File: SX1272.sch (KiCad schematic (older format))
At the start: 33 parts, among them J8 SMA, U7 SX1272, U8 PE4259, Y2 Crystal

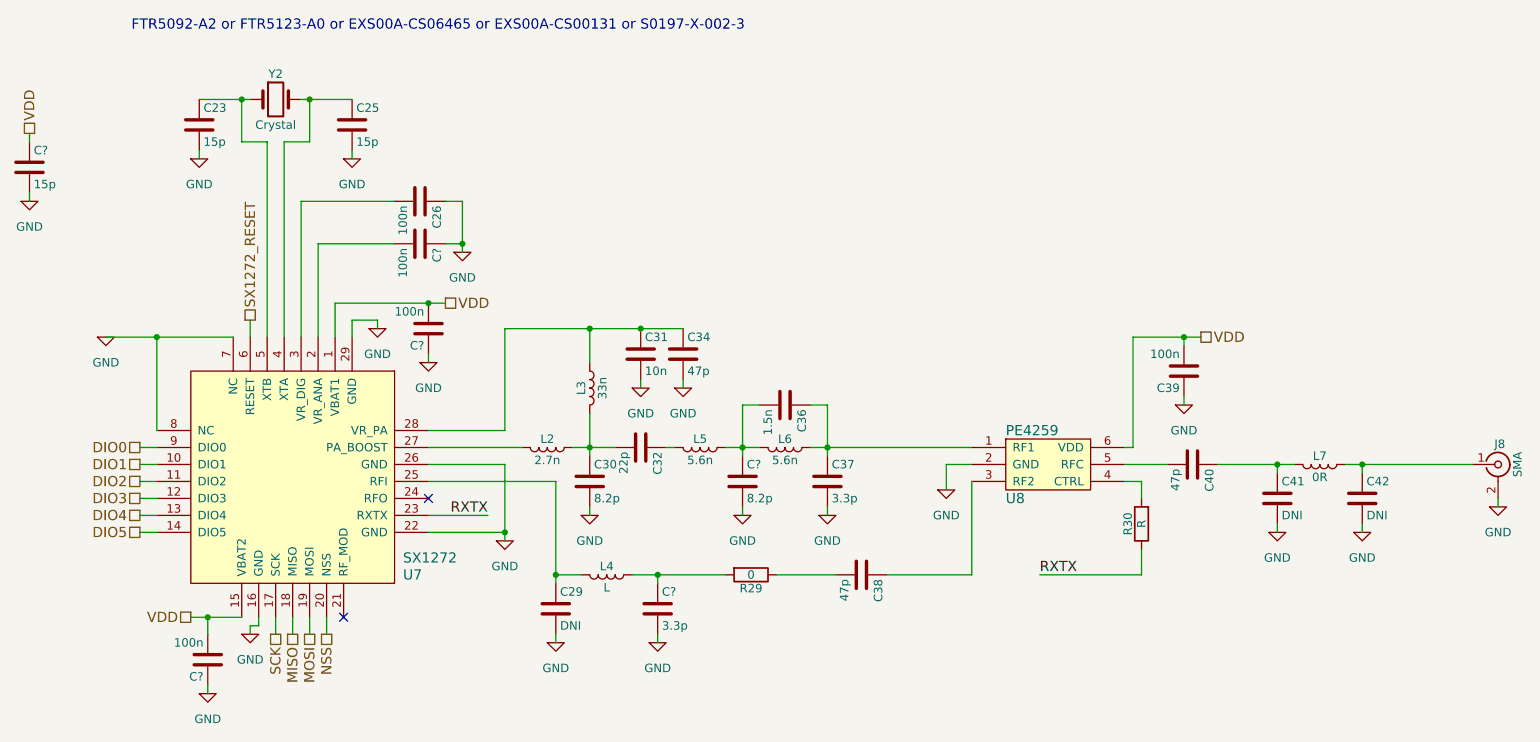
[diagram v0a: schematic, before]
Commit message: Most components arranged on PCB
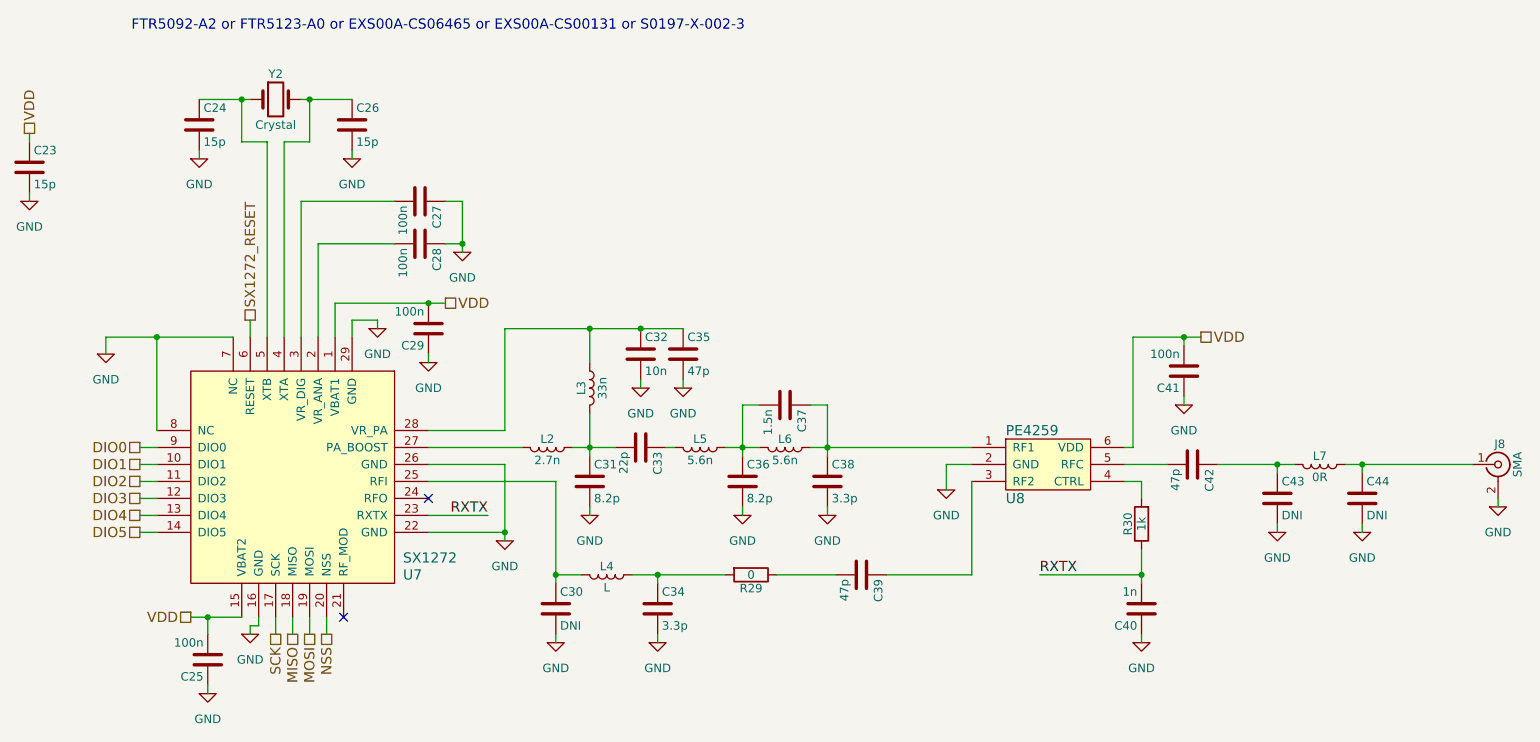
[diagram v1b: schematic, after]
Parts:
- removed C25: 15p, symbol C
- added C26: 15p, Capacitors_SMD:C_0805_HandSoldering, symbol C
- added C40: 1n, Capacitors_SMD:C_0805_HandSoldering, symbol C
- C24: renamed from C23; footprint (none) -> Capacitors_SMD:C_0805_HandSoldering
- C25: renamed from C?; footprint Capacitors_SMD:C_0402_NoSilk -> Capacitors_SMD:C_0805_NoSilk
- J8: footprint footprints:RP-SMA -> tracking_device:RP-SMA
- L2, L3, L4, L5, L6, L7: footprint footprints:L_0402_NoSilk -> tracking_device:L_0402_NoSilk
- R30: value R -> 1k
- U8: footprint footprints:SOT-363_SC-70-6_Handsoldering -> tracking_device:SOT-363_SC-70-6_Handsoldering
- Y2: footprint (none) -> Crystals:Crystal_SMD_2012-2pin_2.0x1.2mm_HandSoldering
- gave numbers to parts that had none: 5
- renumbered C26 to C27, C29 to C30, C30 to C31, C31 to C32, C32 to C33, C34 to C35, C36 to C37, C37 to C38, C38 to C39, C39 to C41, C40 to C42, C41 to C43, C42 to C44
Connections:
- net GND: now also C26.2, C40.1
- net RXTX: now also C40.2
- net at U7.4 (XTA), Y2.2: now also C26.1

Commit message: Added RFM95W
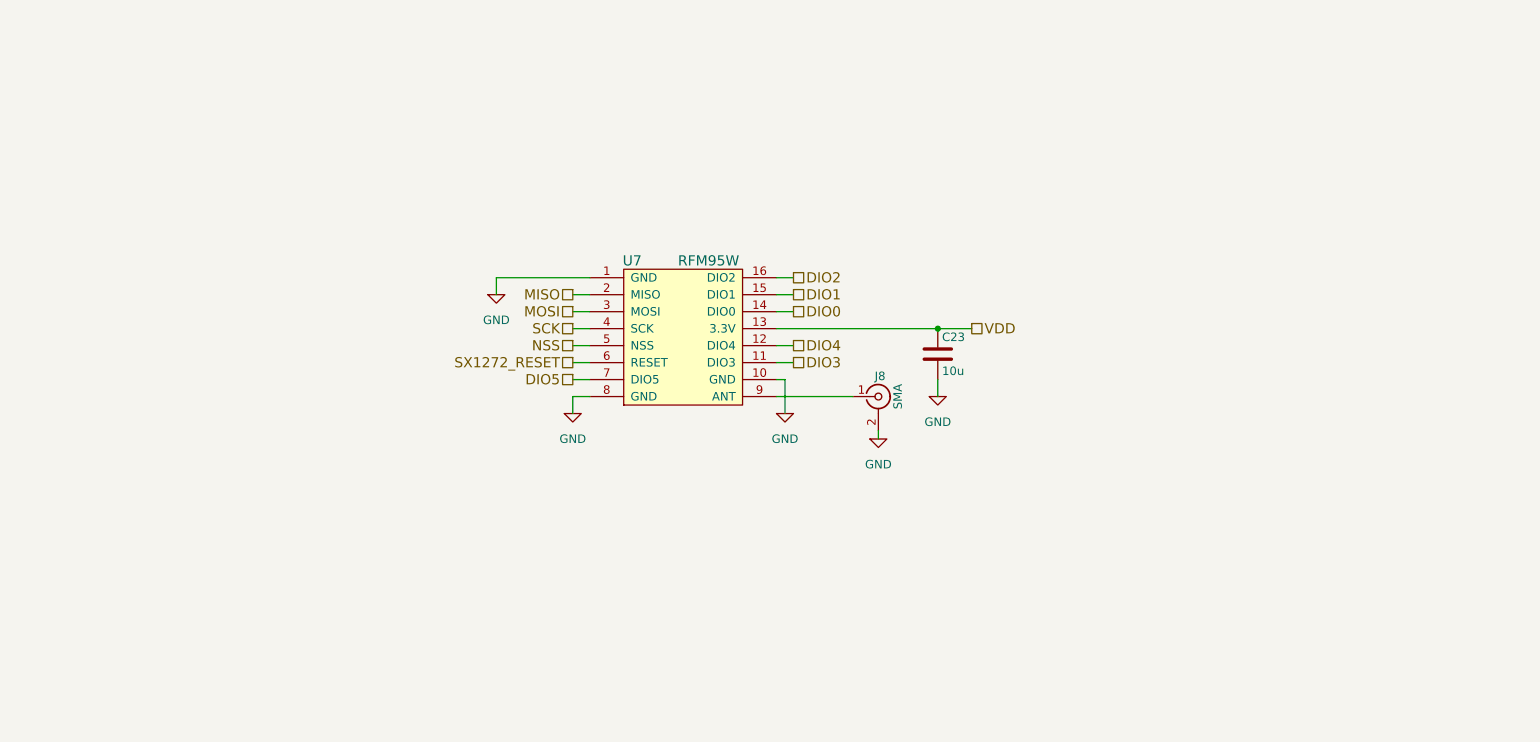
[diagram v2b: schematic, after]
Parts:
- removed C24, C26: 15p, Capacitors_SMD:C_0805_HandSoldering, symbol C
- removed C25: 100n, Capacitors_SMD:C_0805_NoSilk, symbol C
- removed C27, C28, C29, C41: 100n, Capacitors_SMD:C_0402_NoSilk, symbol C
- removed C30, C43, C44: DNI, Capacitors_SMD:C_0402_NoSilk, symbol C
- removed C31, C36: 8.2p, Capacitors_SMD:C_0402_NoSilk, symbol C
- removed C32: 10n, Capacitors_SMD:C_0402_NoSilk, symbol C
- removed C33: 22p, Capacitors_SMD:C_0402_NoSilk, symbol C
- removed C34, C38: 3.3p, Capacitors_SMD:C_0402_NoSilk, symbol C
- removed C35, C42: 47p, Capacitors_SMD:C_0402_NoSilk, symbol C
- removed C37: 1.5n, Capacitors_SMD:C_0402_NoSilk, symbol C
- removed C39: 47p, Resistors_SMD:R_0402_NoSilk, symbol C
- removed C40: 1n, Capacitors_SMD:C_0805_HandSoldering, symbol C
- removed L2: 2.7n, tracking_device:L_0402_NoSilk, symbol L
- removed L3: 33n, tracking_device:L_0402_NoSilk, symbol L
- removed L4: L, tracking_device:L_0402_NoSilk, symbol L
- removed L5, L6: 5.6n, tracking_device:L_0402_NoSilk, symbol L
- removed L7: 0R, tracking_device:L_0402_NoSilk, symbol L
- removed R29: 0, Resistors_SMD:R_0402_NoSilk, symbol R
- removed R30: 1k, Resistors_SMD:R_0805_HandSoldering, symbol R
- removed U7: SX1272, Housings_DFN_QFN:QFN-28-1EP_6x6mm_Pitch0.65mm, symbol SX1272
- removed U8: PE4259, tracking_device:SOT-363_SC-70-6_Handsoldering, symbol PE4259
- removed Y2: Crystal, Crystals:Crystal_SMD_2012-2pin_2.0x1.2mm_HandSoldering, symbol Crystal
- added U7: RFM95W, tracking_device:RFM95W, symbol RFM95W
- C23: value 15p -> 10u
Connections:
- net DIO0: now also U7.14 (DIO0)
- net DIO1: now also U7.15 (DIO1)
- net DIO2: now also U7.16 (DIO2)
- net DIO3: now also U7.11 (DIO3)
- net DIO4: now also U7.12 (DIO4)
- net DIO5: now also U7.7 (DIO5)
- net GND: now also U7.1 (GND), U7.10 (GND), U7.8 (GND)
- net MISO: now also U7.2 (MISO)
- net MOSI: now also U7.3 (MOSI)
- net NSS: now also U7.5 (NSS)
- net SCK: now also U7.4 (SCK)
- net SX1272_RESET: now also U7.6 (RESET)
- net VDD: now also U7.13 (3.3V)
- net at J8.1 (In): now also U7.9 (ANT)
- no-connect marks 2 -> 0
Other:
- note removed: "FTR5092-A2 or FTR5123-A0 or EXS00A-CS06465 or EXS00A-CS00131 or S0197-X-002-3"
- moved on the sheet: J8

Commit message: Version sent out for fabrication
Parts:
- renumbered J8 to J11
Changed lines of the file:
@@
 LIBS:tracking_device
 LIBS:RF_Modules
+LIBS:Electromechanical
+LIBS:Test_Point
+LIBS:electomech-misc
+LIBS:_electromech
+LIBS:Mounting_Hole
 LIBS:tracking_device-cache
 EELAYER 25 0
@@
 SX1272_RESET
 $Comp
-L CONN_COAXIAL J8
+L CONN_COAXIAL J11
 U 1 1 59B49CF4
 P 6200 3550
-F 0 "J8" H 6210 3670 50  0000 C CNN
+F 0 "J11" H 6210 3670 50  0000 C CNN
 F 1 "SMA" V 6315 3550 50  0000 C CNN
 F 2 "tracking_device:RP-SMA" H 6200 3550 50  0001 C CNN
 F 3 "" H 6200 3550 50  0001 C CNN
 	1    6200 3550
-	1    0    0    -1
-$EndComp
-$Comp
-L GND #PWR039
-U 1 1 59B49DE3
-P 6200 3800
-F 0 "#PWR039" H 6200 3550 50  0001 C CNN
-F 1 "GND" H 6200 3650 50  0000 C CNN
-F 2 "" H 6200 3800 50  0001 C CNN
-F 3 "" H 6200 3800 50  0001 C CNN
-	1    6200 3800
 	1    0    0    -1
 $EndComp
@@
 $EndComp
 $Comp
-L GND #PWR040
-U 1 1 59ED90BA
-P 5650 3650
-F 0 "#PWR040" H 5650 3400 50  0001 C CNN
-F 1 "GND" H 5650 3500 50  0000 C CNN
-F 2 "" H 5650 3650 50  0001 C CNN
-F 3 "" H 5650 3650 50  0001 C CNN
-	1    5650 3650
-	1    0    0    -1
-$EndComp
-$Comp
-L GND #PWR041
-U 1 1 59ED90CB
-P 4400 3650
-F 0 "#PWR041" H 4400 3400 50  0001 C CNN
-F 1 "GND" H 4400 3500 50  0000 C CNN
-F 2 "" H 4400 3650 50  0001 C CNN
-F 3 "" H 4400 3650 50  0001 C CNN
-	1    4400 3650
-	1    0    0    -1
-$EndComp
-$Comp
-L GND #PWR042
-U 1 1 59ED90DC
-P 3950 2950
-F 0 "#PWR042" H 3950 2700 50  0001 C CNN
-F 1 "GND" H 3950 2800 50  0000 C CNN
-F 2 "" H 3950 2950 50  0001 C CNN
-F 3 "" H 3950 2950 50  0001 C CNN
-	1    3950 2950
-	1    0    0    -1
-$EndComp
-$Comp
 L C C23
 U 1 1 59EDA1E2
@@
 $EndComp
 Wire Wire Line
-	6200 3800 6200 3750
-Wire Wire Line
 	6050 3550 5600 3550
 Wire Wire Line
-	3950 2950 3950 2850
-Wire Wire Line
-	3950 2850 4500 2850
-Wire Wire Line
-	4400 3650 4400 3550
-Wire Wire Line
-	4400 3550 4500 3550
-Wire Wire Line
-	5650 3650 5650 3450
-Wire Wire Line
-	5650 3450 5600 3450
+	5600 3450 6150 3450
 Wire Wire Line
 	5600 2850 5700 2850
@@
 	4500 2950 4400 2950
 Connection ~ 6550 3150
-$Comp
-L GND #PWR043
-U 1 1 59EDA2EC
-P 6550 3550
-F 0 "#PWR043" H 6550 3300 50  0001 C CNN
-F 1 "GND" H 6550 3400 50  0000 C CNN
-F 2 "" H 6550 3550 50  0001 C CNN
-F 3 "" H 6550 3550 50  0001 C CNN
-	1    6550 3550
-	1    0    0    -1
-$EndComp
 Wire Wire Line
-	6550 3550 6550 3450
+	6550 3850 6550 3450
+Text HLabel 5550 3850 0    60   UnSpc ~ 0
+GND
+Text Label 6100 3850 2    60   ~ 0
+RADIO_GND
+Wire Wire Line
+	5550 3850 6550 3850
+Text Label 6150 3450 2    60   ~ 0
+RADIO_GND
+Text Label 3950 3600 0    60   ~ 0
+RADIO_GND
+Text Label 4000 2850 0    60   ~ 0
+RADIO_GND
+Wire Wire Line
+	4500 2850 4000 2850
+Wire Wire Line
+	4500 3550 4500 3600
+Wire Wire Line
+	4500 3600 3950 3600
+Wire Wire Line
+	6200 3750 6200 3850
+Connection ~ 6200 3850
 $EndSCHEMATC

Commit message: Working on rev 3, started board layout
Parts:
- removed J11: SMA, tracking_device:RP-SMA, symbol CONN_COAXIAL
- added C22, C23: 10u, Capacitors_SMD:C_0805_HandSoldering, symbol C
- added L1: L, Inductors_SMD:L_0805_HandSoldering, symbol L
- renumbered C23 to C24
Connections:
- net at U7.9 (ANT): now also C22.1, L1.2
- net GND renamed RADIO_GND
- net RADIO_GND: now also C22.2, C23.2
- new net ANTENNA: C23.1, L1.1
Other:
- note added: "Antenna from app note DN024 from TI"
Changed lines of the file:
@@
 Text HLabel 4400 3350 0    60   UnSpc ~ 0
 SX1272_RESET
-$Comp
-L CONN_COAXIAL J11
-U 1 1 59B49CF4
-P 6200 3550
-F 0 "J11" H 6210 3670 50  0000 C CNN
-F 1 "SMA" V 6315 3550 50  0000 C CNN
-F 2 "tracking_device:RP-SMA" H 6200 3550 50  0001 C CNN
-F 3 "" H 6200 3550 50  0001 C CNN
-	1    6200 3550
-	1    0    0    -1
-$EndComp
 Text HLabel 4400 3150 0    60   UnSpc ~ 0
 SCK
@@
 VDD
 $Comp
-L RFM95W U7
-U 1 1 59ED83FF
-P 4700 3600
-F 0 "U7" H 4750 4450 60  0000 C CNN
-F 1 "RFM95W" H 5200 4450 60  0000 C CNN
-F 2 "tracking_device:RFM95W" H 5200 4450 60  0001 C CNN
-F 3 "" H 5200 4450 60  0001 C CNN
-	1    4700 3600
-	1    0    0    -1
-$EndComp
-$Comp
-L C C23
+L C C24
 U 1 1 59EDA1E2
 P 6550 3300
-F 0 "C23" H 6575 3400 50  0000 L CNN
+F 0 "C24" H 6575 3400 50  0000 L CNN
 F 1 "10u" H 6575 3200 50  0000 L CNN
 F 2 "Capacitors_SMD:C_0805_HandSoldering" H 6588 3150 50  0001 C CNN
@@
 	1    0    0    -1
 $EndComp
-Wire Wire Line
-	6050 3550 5600 3550
 Wire Wire Line
 	5600 3450 6150 3450
@@
 	4500 2950 4400 2950
 Connection ~ 6550 3150
-Wire Wire Line
-	6550 3850 6550 3450
-Text HLabel 5550 3850 0    60   UnSpc ~ 0
-GND
-Text Label 6100 3850 2    60   ~ 0
-RADIO_GND
-Wire Wire Line
-	5550 3850 6550 3850
 Text Label 6150 3450 2    60   ~ 0
 RADIO_GND
@@
 Wire Wire Line
 	4500 3600 3950 3600
+$Comp
+L RFM95W U7
+U 1 1 59ED83FF
+P 4700 3600
+F 0 "U7" H 4750 4450 60  0000 C CNN
+F 1 "RFM95W" H 5200 4450 60  0000 C CNN
+F 2 "tracking_device:RFM95W" H 5200 4450 60  0001 C CNN
+F 3 "" H 5200 4450 60  0001 C CNN
+	1    4700 3600
+	1    0    0    -1
+$EndComp
+Text Label 7150 3550 2    60   ~ 0
+RADIO_GND
 Wire Wire Line
-	6200 3750 6200 3850
-Connection ~ 6200 3850
+	7150 3550 6550 3550
+Wire Wire Line
+	6550 3550 6550 3450
+Text Label 6900 3850 2    60   ~ 0
+ANTENNA
+Text Notes 3350 5150 0    60   ~ 0
+Antenna from app note DN024 from TI
+$Comp
+L C C23
+U 1 1 5ACC1A63
+P 6400 4050
+F 0 "C23" H 6425 4150 50  0000 L CNN
+F 1 "10u" H 6425 3950 50  0000 L CNN
+F 2 "Capacitors_SMD:C_0805_HandSoldering" H 6438 3900 50  0001 C CNN
+F 3 "" H 6400 4050 50  0001 C CNN
+	1    6400 4050
+	1    0    0    -1
+$EndComp
+$Comp
+L C C22
+U 1 1 5ACC1A98
+P 5900 4050
+F 0 "C22" H 5925 4150 50  0000 L CNN
+F 1 "10u" H 5925 3950 50  0000 L CNN
+F 2 "Capacitors_SMD:C_0805_HandSoldering" H 5938 3900 50  0001 C CNN
+F 3 "" H 5900 4050 50  0001 C CNN
+	1    5900 4050
+	1    0    0    -1
+$EndComp
+$Comp
+L L L1
+U 1 1 5ACC1AC3
+P 6150 3850
+F 0 "L1" V 6100 3850 50  0000 C CNN
+F 1 "L" V 6225 3850 50  0000 C CNN
+F 2 "Inductors_SMD:L_0805_HandSoldering" H 6150 3850 50  0001 C CNN
+F 3 "" H 6150 3850 50  0001 C CNN
+	1    6150 3850
+	0    1    1    0
+$EndComp
+Wire Wire Line
+	6900 3850 6300 3850
+Wire Wire Line
+	6400 3900 6400 3850
+Connection ~ 6400 3850
+Wire Wire Line
+	5900 3900 5900 3850
+Wire Wire Line
+	5600 3850 6000 3850
+Wire Wire Line
+	5600 3850 5600 3550
+Connection ~ 5900 3850
+Text Label 7000 4300 2    60   ~ 0
+RADIO_GND
+Wire Wire Line
+	5900 4300 7000 4300
+Wire Wire Line
+	6400 4300 6400 4200
+Wire Wire Line
+	5900 4300 5900 4200
+Connection ~ 6400 4300
 $EndSCHEMATC

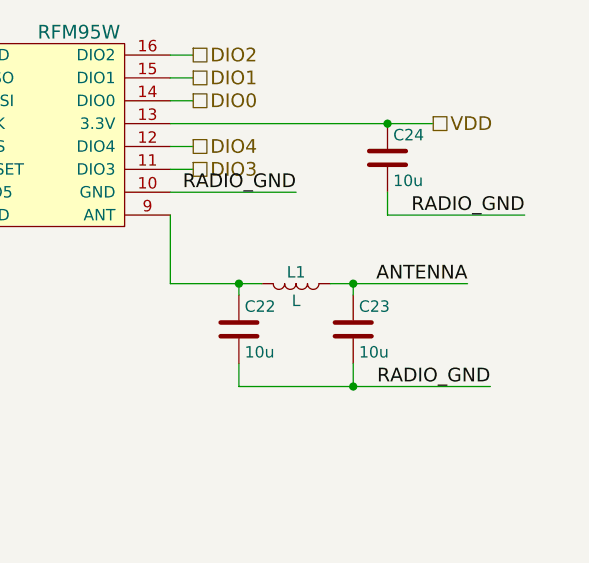
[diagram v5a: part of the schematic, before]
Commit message: Rev 3 DRC clean
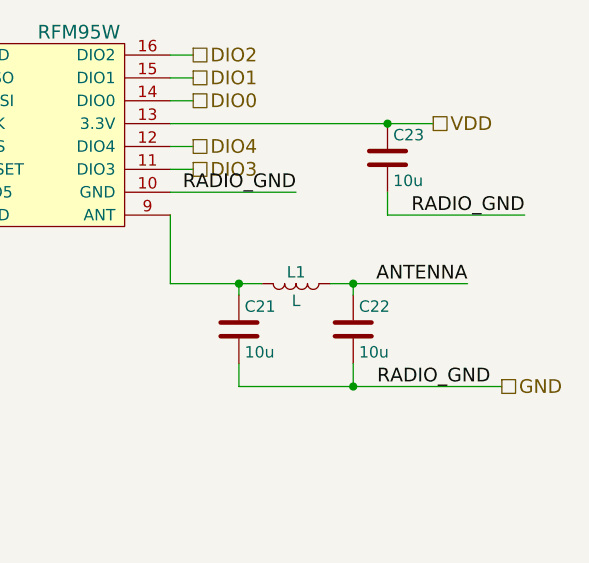
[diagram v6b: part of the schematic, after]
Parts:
- renumbered C22 to C21, C23 to C22, C24 to C23
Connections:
- net RADIO_GND renamed GND
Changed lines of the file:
@@
 VDD
 $Comp
-L C C24
+L C C23
 U 1 1 59EDA1E2
 P 6550 3300
-F 0 "C24" H 6575 3400 50  0000 L CNN
+F 0 "C23" H 6575 3400 50  0000 L CNN
 F 1 "10u" H 6575 3200 50  0000 L CNN
 F 2 "Capacitors_SMD:C_0805_HandSoldering" H 6588 3150 50  0001 C CNN
@@
 Antenna from app note DN024 from TI
 $Comp
-L C C23
+L C C22
 U 1 1 5ACC1A63
 P 6400 4050
-F 0 "C23" H 6425 4150 50  0000 L CNN
+F 0 "C22" H 6425 4150 50  0000 L CNN
 F 1 "10u" H 6425 3950 50  0000 L CNN
 F 2 "Capacitors_SMD:C_0805_HandSoldering" H 6438 3900 50  0001 C CNN
@@
 $EndComp
 $Comp
-L C C22
+L C C21
 U 1 1 5ACC1A98
 P 5900 4050
-F 0 "C22" H 5925 4150 50  0000 L CNN
+F 0 "C21" H 5925 4150 50  0000 L CNN
 F 1 "10u" H 5925 3950 50  0000 L CNN
 F 2 "Capacitors_SMD:C_0805_HandSoldering" H 5938 3900 50  0001 C CNN
@@
 RADIO_GND
 Wire Wire Line
-	5900 4300 7000 4300
+	5900 4300 7050 4300
 Wire Wire Line
 	6400 4300 6400 4200
@@
 	5900 4300 5900 4200
 Connection ~ 6400 4300
+Text HLabel 7050 4300 2    60   UnSpc ~ 0
+GND
 $EndSCHEMATC
